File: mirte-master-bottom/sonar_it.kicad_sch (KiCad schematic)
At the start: 3 parts, among them J1 sonar_conn

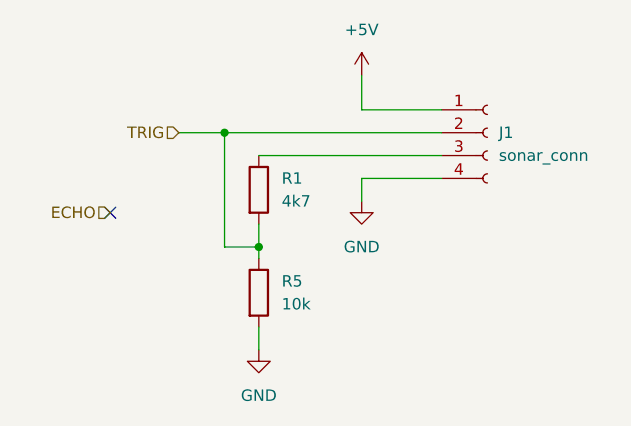
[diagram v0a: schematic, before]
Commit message: Cleanups, text fixes for 3rd test pcb with assembly
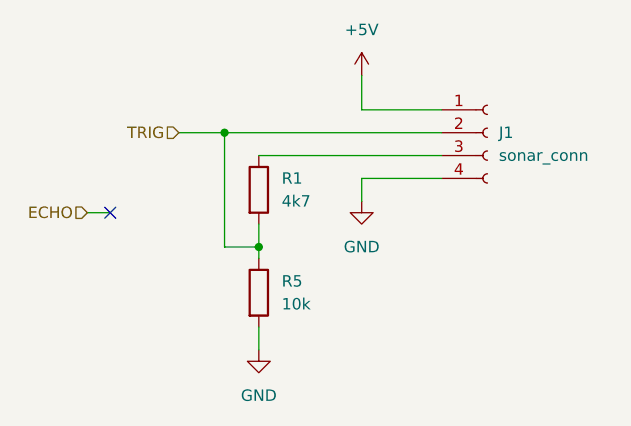
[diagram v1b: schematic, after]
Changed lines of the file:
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@@
+	(wire
+		(pts
+			(xy 123.19 88.9) (xy 125.73 88.9)
+		)
+		(stroke
+			(width 0)
+			(type default)
+		)
+	)
 	(wire
 		(pts
@@
 	(hierarchical_label "ECHO"
 		(shape input)
-		(at 125.73 88.9 180)
+		(at 123.19 88.9 180)
 		(effects
 			(font
